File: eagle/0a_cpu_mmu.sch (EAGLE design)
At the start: 9 parts

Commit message: Parts library updated (added fast SRAM), MMU board half complete
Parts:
- added IC1, IC2: MT5C6408, dawid:MT5C6408
- added IC10, IC11, IC12, IC13, IC14, IC9: 74LS157N, 74xx-eu:74LS157N
- added IC15: 74LS04N, 74xx-eu:74LS04N
- added IC3: 74LS27N, 74xx-eu:74LS27N
- added IC4: 74LS20N, 74xx-eu:74LS20N
- added IC5: 74LS08N, 74xx-eu:74LS08N
- added IC6, IC7: 74LS245N, 74xx-eu:74LS245N
- added IC8: 74LS32N, 74xx-eu:74LS32N
- added JP5: (no value), pinhead:PINHD-2X5
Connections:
- new net /ENPTAB: IC14A.4A, IC6A.DIR, IC7A.DIR, IC8B.O
- new net /LDPTAB: IC1G$1.!WE, IC2G$1.!WE, IC8A.O
- new net /PTAB: IC13A.!A!/B, IC14A.!A!/B, IC4A.O, IC8A.I0, IC8B.I0, IC8C.I0, IC8D.I0
- new net N$1: IC3A.O, IC4A.I0
- new net N$10: IC10A.2A, IC1G$1.DQ6, IC6A.A6
- new net N$11: IC10A.3A, IC1G$1.DQ7, IC6A.A7
- new net N$12: IC10A.4A, IC1G$1.DQ8, IC6A.A8
- new net N$13: IC2G$1.DQ1, IC7A.A1
- new net N$14: IC2G$1.DQ2, IC7A.A2
- new net N$15: IC2G$1.DQ3, IC7A.A3
- new net N$16: IC2G$1.DQ4, IC7A.A4
- new net N$17: IC2G$1.DQ5, IC7A.A5
- new net N$18: IC2G$1.DQ6, IC7A.A6
- new net N$19: IC2G$1.DQ7, IC7A.A7
- new net N$2: IC3B.O, IC4A.I1
- new net N$20: IC2G$1.DQ8, IC7A.A8
- new net N$21: IC13A.1Y, IC1G$1.A0, IC2G$1.A0
- new net N$22: IC13A.2Y, IC1G$1.A1, IC2G$1.A1
- new net N$23: IC13A.3Y, IC1G$1.A2, IC2G$1.A2
- new net N$24: IC13A.4Y, IC1G$1.A3, IC2G$1.A3
- new net N$25: IC14A.1Y, IC1G$1.A4, IC2G$1.A4
- new net N$26: IC14A.2Y, IC1G$1.A5, IC2G$1.A5
- new net N$27: IC1G$1.CE2, IC7A.G, IC8C.O
- new net N$28: IC2G$1.CE2, IC6A.G, IC8D.O
- new net N$29: IC14A.4Y, IC1G$1.!OE, IC2G$1.!OE
- new net N$3: IC3C.O, IC4A.I2
- new net N$30: IC15A.O, IC8C.I1
- new net N$4: IC4A.I3, IC5A.O
- new net N$5: IC1G$1.DQ1, IC6A.A1, IC9A.1A
- new net N$6: IC1G$1.DQ2, IC6A.A2, IC9A.2A
- new net N$7: IC1G$1.DQ3, IC6A.A3, IC9A.3A
- new net N$8: IC1G$1.DQ4, IC6A.A4, IC9A.4A
- new net N$9: IC10A.1A, IC1G$1.DQ5, IC6A.A5
- new net PABUS12: JP5.1
- new net PABUS13: JP5.2
- new net PABUS14: JP5.3
- new net PABUS15: JP5.4
- new net PABUS16: JP5.5
- new net PABUS17: JP5.6
- new net PABUS18: JP5.7
- new net PABUS19: JP5.8
- new net PABUS20: JP5.9
- new net PABUS21: JP5.10
- net /ENMEM: now also IC8B.I1
- net /FS: now also IC14A.2B, IC3C.I2
- net /LDMEM: now also IC8A.I1
- net ABUS0: now also IC15A.I, IC8D.I1
- net ABUS1: now also IC13A.1A
- net ABUS10: now also IC3A.I2
- net ABUS11: now also IC3B.I0
- net ABUS12: now also IC13A.1B, IC3B.I1
- net ABUS13: now also IC13A.2B, IC3B.I2
- net ABUS14: now also IC13A.3B, IC3C.I0
- net ABUS15: now also IC13A.4B, IC3C.I1
- net ABUS2: now also IC13A.2A
- net ABUS3: now also IC13A.3A
- net ABUS4: now also IC13A.4A
- net ABUS5: now also IC14A.1A
- net ABUS6: now also IC14A.2A
- net ABUS7: now also IC5A.I0
- net ABUS8: now also IC3A.I0
- net ABUS9: now also IC3A.I1
- net DBUS0: now also IC6A.B1, IC7A.B1
- net DBUS1: now also IC6A.B2, IC7A.B2
- net DBUS2: now also IC6A.B3, IC7A.B3
- net DBUS3: now also IC6A.B4, IC7A.B4
- net DBUS4: now also IC6A.B5, IC7A.B5
- net DBUS5: now also IC6A.B6, IC7A.B6
- net DBUS6: now also IC6A.B7, IC7A.B7
- net DBUS7: now also IC6A.B8, IC7A.B8
- net GND: now also IC10A.1B, IC10A.2B, IC10A.3B, IC10A.4B, IC13A.G, IC14A.4B, IC14A.G, IC1G$1.!CE1, IC1G$1.A10, IC1G$1.A11, IC1G$1.A12, IC1G$1.A6, IC1G$1.A7, IC1G$1.A8, IC1G$1.A9, IC2G$1.!CE1, IC2G$1.A10, IC2G$1.A11, IC2G$1.A12, IC2G$1.A6, IC2G$1.A7, IC2G$1.A8, IC2G$1.A9, IC9A.1B, IC9A.2B, IC9A.3B, IC9A.4B
- net MEMSEG: now also IC14A.1B, IC5A.I1

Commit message: MMU schematics update
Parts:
- added IC16: 74LS04N, 74xx-eu:74LS04N
- added IC17: 74LS32N, 74xx-eu:74LS32N
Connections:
- new net /ENMEMX: IC12A.1Y
- new net /LDMEMX: IC12A.2Y
- new net FIO: IC16A.I, IC2G$1.DQ6, IC7A.A6
- new net FPRESENT: IC17D.I0, IC2G$1.DQ8, IC7A.A8
- new net FWRITABLE: IC17C.I0, IC2G$1.DQ7, IC7A.A7
- new net N$31: IC12A.3B, IC17B.O
- new net N$32: IC12A.4B, IC17A.O
- new net N$33: IC17B.I0, IC17C.O
- new net N$34: IC17A.I0, IC17D.O
- net +5V: now also IC11A.3B, IC12A.1A, IC12A.2A, IC12A.3A, IC12A.4A
- net /ENMEM: now also IC12A.1B, IC17A.I1
- net /FP: now also IC10A.!A!/B, IC11A.!A!/B, IC17C.I1, IC17D.I1, IC9A.!A!/B
- net /IO: now also IC11A.3Y
- net /LDMEM: now also IC17B.I1
- net /NP_FAULT: now also IC12A.4Y
- net /PTAB: now also IC12A.!A!/B; no longer IC13A.!A!/B, IC14A.!A!/B, IC4A.O, IC8A.I0, IC8B.I0, IC8C.I0, IC8D.I0
- net /WR_FAULT: now also IC12A.3Y
- net GND: now also IC10A.G, IC11A.1B, IC11A.2B, IC11A.G, IC12A.G, IC9A.G
- net N$13: now also IC11A.1A
- net N$14: now also IC11A.2A
- net N$18: now also IC11A.3A, IC16A.O; no longer IC2G$1.DQ6, IC7A.A6
- net N$19: now also IC13A.!A!/B, IC14A.!A!/B, IC4A.O, IC8A.I0, IC8B.I0, IC8C.I0, IC8D.I0; no longer IC2G$1.DQ7, IC7A.A7
- net N$20: now also IC12A.2B; no longer IC2G$1.DQ8, IC7A.A8
- net PABUS12: now also IC9A.1Y
- net PABUS13: now also IC9A.2Y
- net PABUS14: now also IC9A.3Y
- net PABUS15: now also IC9A.4Y
- net PABUS16: now also IC10A.1Y
- net PABUS17: now also IC10A.2Y
- net PABUS18: now also IC10A.3Y
- net PABUS19: now also IC10A.4Y
- net PABUS20: now also IC11A.1Y
- net PABUS21: now also IC11A.2Y
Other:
- note added: "Inhibit write on WR_FAULT"
- moved on the sheet: IC1, IC10, IC11, IC12, IC13, IC14, IC15A, IC1P, IC2, IC2P, IC3A, IC3B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

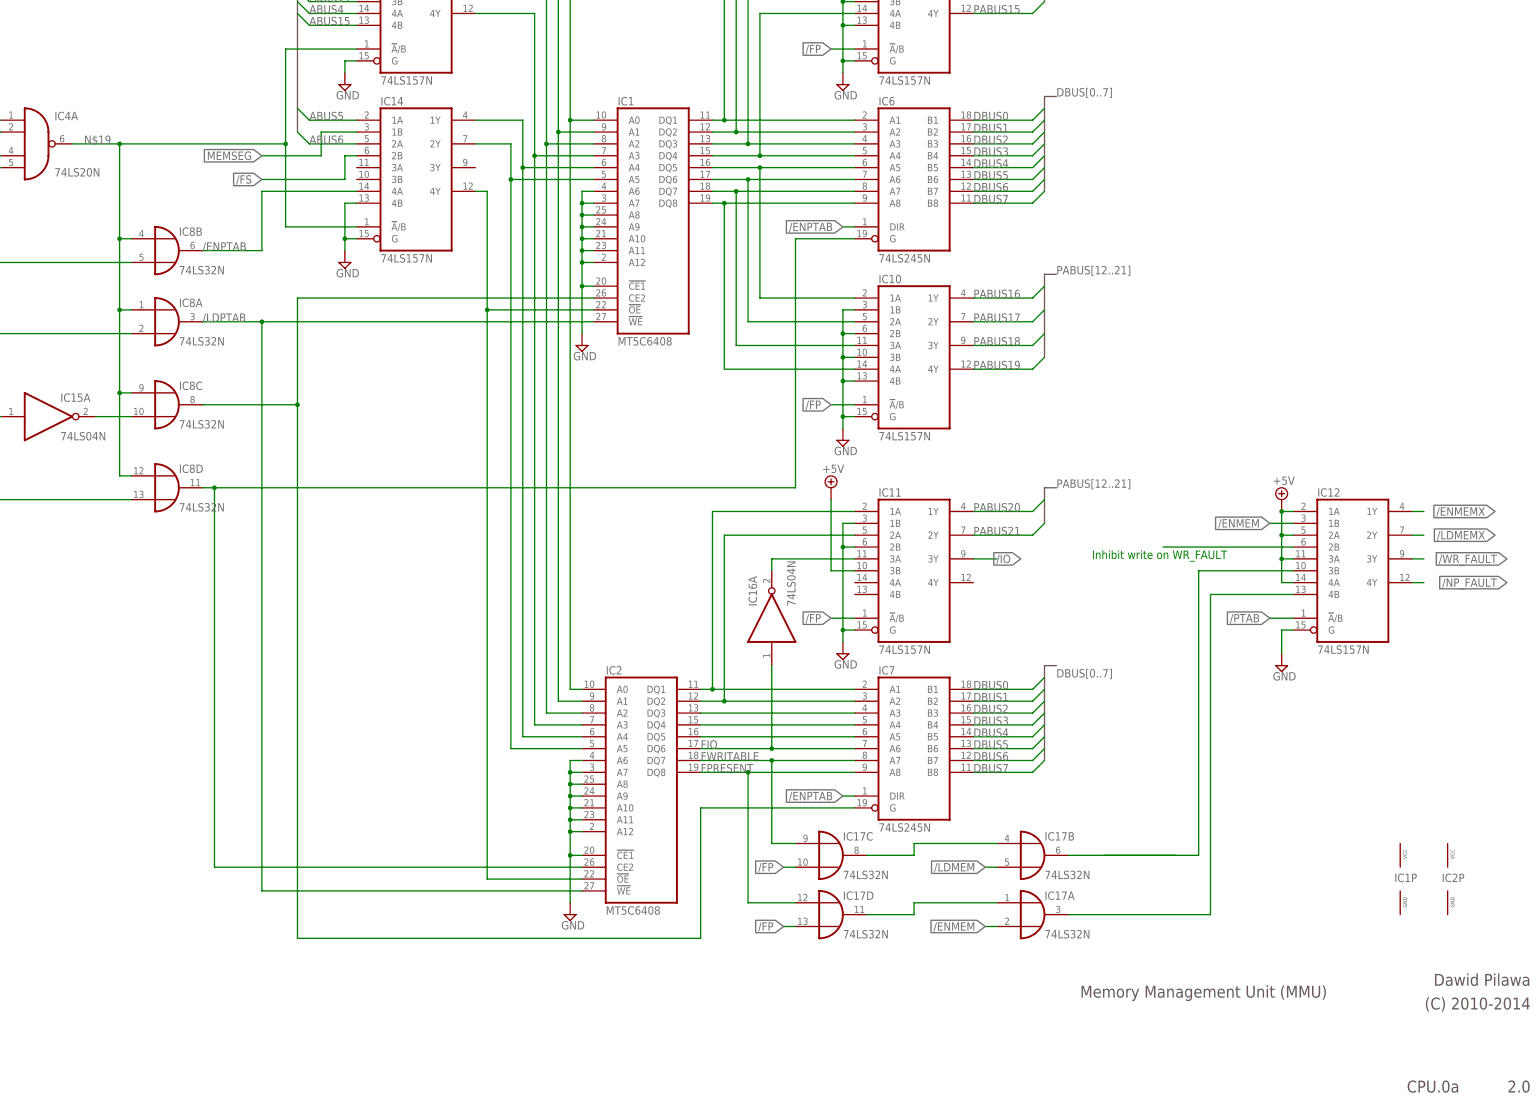
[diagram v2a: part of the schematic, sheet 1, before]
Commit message: Updates to MMU faults generation circuit
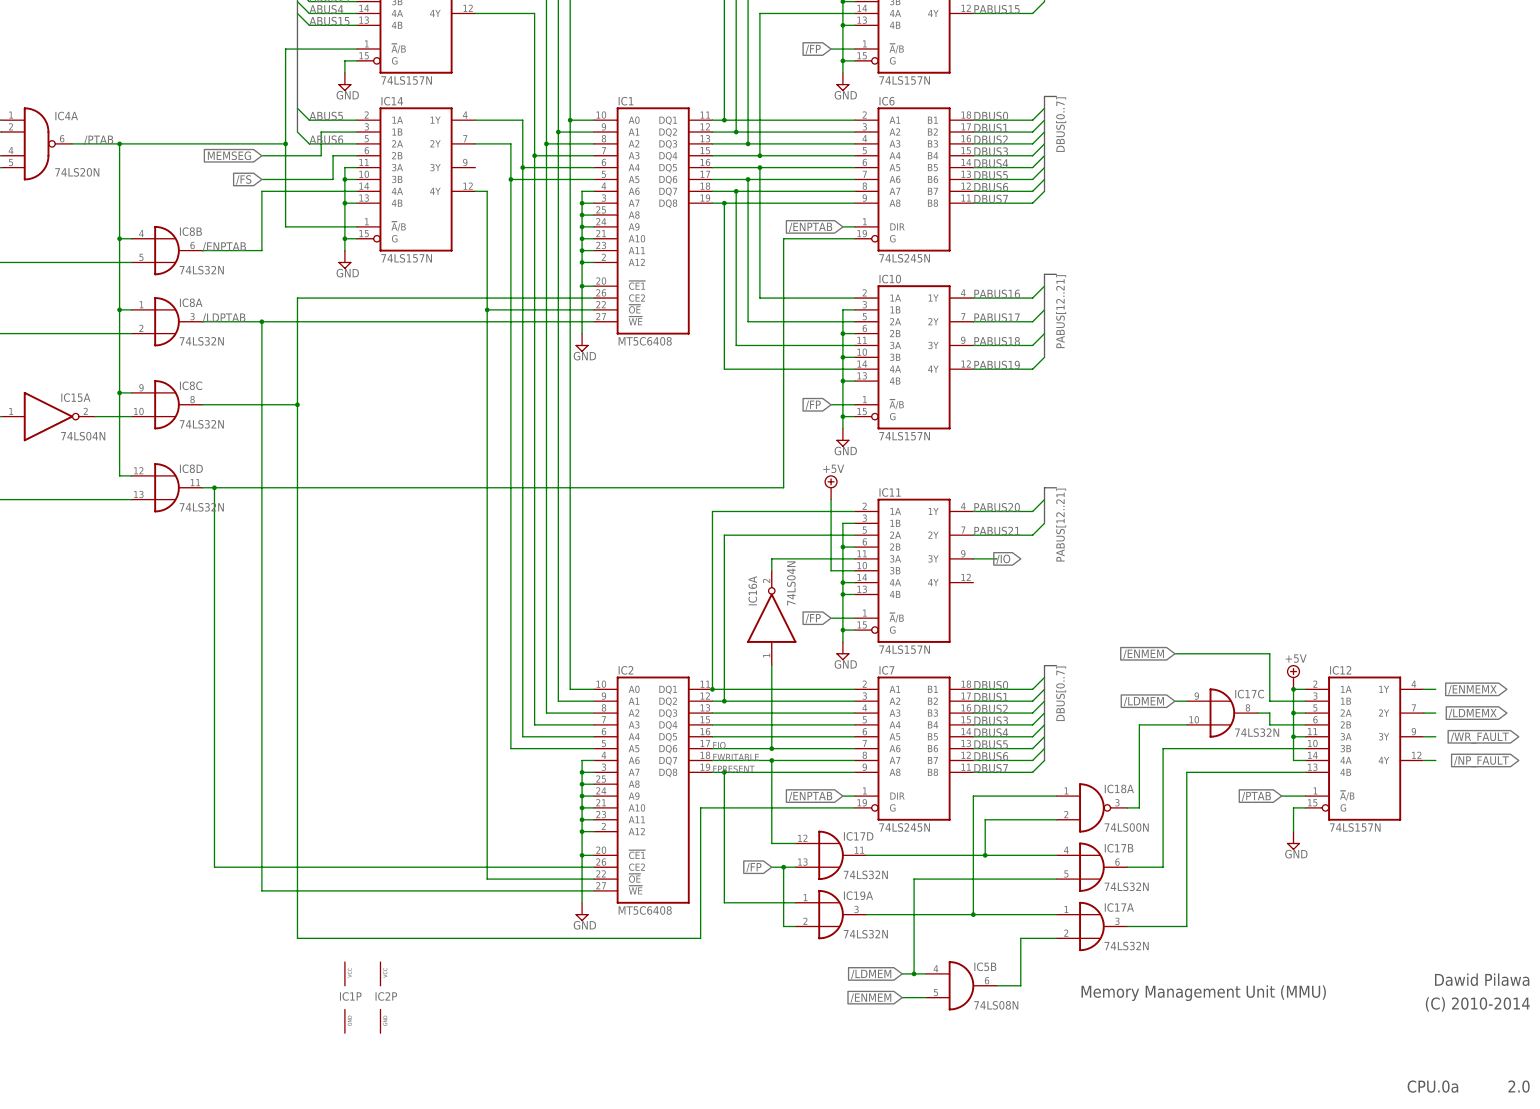
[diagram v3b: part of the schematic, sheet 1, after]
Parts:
- added IC18: 74LS00N, 74xx-eu:74LS00N
- added IC19: 74LS32N, 74xx-eu:74LS32N
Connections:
- new net N$35: IC17A.I0, IC18A.I0, IC19A.O
- net /ENMEM: now also IC5B.I1; no longer IC17A.I1
- net /FP: now also IC19A.I1; no longer IC17C.I1
- net /LDMEM: now also IC17C.I0, IC5B.I0
- net /PTAB: now also IC13A.!A!/B, IC14A.!A!/B, IC4A.O, IC8A.I0, IC8B.I0, IC8C.I0, IC8D.I0
- net FPRESENT: now also IC19A.I0; no longer IC17D.I0
- net FWRITABLE: now also IC17D.I0; no longer IC17C.I0
- net GND: now also IC11A.4A, IC11A.4B, IC14A.3A, IC14A.3B
- net N$19: now also IC17A.I1, IC5B.O; no longer IC13A.!A!/B, IC14A.!A!/B, IC4A.O, IC8A.I0, IC8B.I0, IC8C.I0, IC8D.I0
- net N$20: now also IC17C.O
- net N$33: now also IC17C.I1, IC18A.O; no longer IC17B.I0, IC17C.O
- net N$34: now also IC17B.I0, IC18A.I1; no longer IC17A.I0
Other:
- note removed: "Inhibit write on WR_FAULT"
- moved on the sheet: IC12, IC17A, IC17B, IC17C, IC17D, IC1P, IC2, IC2P

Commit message: More MMU changes, added PPREG
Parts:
- removed IC16: 74LS04N, 74xx-eu:74LS04N
- added IC20: 74LS02N, 74xx-eu:74LS02N
- added IC21: 74LS374N, 74xx-eu:74LS374N
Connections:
- removed net N$3: IC3C.O, IC4A.I2
- new net /PPREG: IC19D.I1, IC4B.O, IC5C.I1
- new net N$37: IC3C.O, IC4A.I2, IC4B.I2
- new net N$39: IC12A.!A!/B, IC5C.O
- new net N$40: IC18C.O, IC19C.I1
- new net N$41: IC19C.O, IC21A.CLK
- new net N$42: IC19D.O, IC21A.OC
- net +5V: now also IC21A.7D, IC21A.8D
- net /ENMEM: now also IC19D.I0
- net /FS: now also IC20B.I1, IC21A.6D
- net /PTAB: now also IC5C.I0; no longer IC12A.!A!/B
- net ABUS12: now also IC21A.1D
- net ABUS13: now also IC21A.2D
- net ABUS14: now also IC21A.3D
- net ABUS15: now also IC21A.4D
- net ABUS7: now also IC20B.I0
- net CLK0A: now also IC19C.I0
- net DBUS0: now also IC21A.1Q
- net DBUS1: now also IC21A.2Q
- net DBUS2: now also IC21A.3Q
- net DBUS3: now also IC21A.4Q
- net DBUS4: now also IC21A.5Q
- net DBUS5: now also IC21A.6Q
- net DBUS6: now also IC21A.7Q
- net DBUS7: now also IC21A.8Q
- net FIO: now also IC15B.I; no longer IC16A.I
- net MEMSEG: now also IC21A.5D
- net N$1: now also IC4B.I0
- net N$18: now also IC15B.O; no longer IC16A.O
- net N$2: now also IC4B.I1
- net N$31: now also IC18C.I0
- net N$32: now also IC18C.I1
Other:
- note added: "(C) 2010-2016"
- moved on the sheet: IC12, IC15A, IC17A, IC17B, IC17C, IC17D, IC18A, IC19A, IC1P, IC2P, IC5B, IC8C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

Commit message: Removal of PPC started
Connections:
- removed net /LDPPC: JP10.11
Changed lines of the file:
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@@
-</segment>
-</net>
-<net name="/LDPPC" class="0">
-<segment>
-<wire x1="83.82" y1="139.7" x2="73.66" y2="139.7" width="0.1524" layer="91"/>
-<pinref part="JP10" gate="A" pin="11"/>
-<label x="73.66" y="139.7" size="1.27" layer="95" rot="R180" xref="yes"/>
 </segment>
 </net>
